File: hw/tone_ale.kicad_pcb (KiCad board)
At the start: 2 copper layers, 99.1 x 72.9 mm, 53 parts, among them J1 Conn_01x02, J2 USB_B_Micro, J3 Conn_01x02, J4 Conn_02x08_Odd_Even, J5 Conn_02x11_Odd_Even, U1 NCP1117-3.3_SOT223, U2 W25Q128JVS, U3 RP2040, U4 PCM5102, U5 PCM1808PWR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

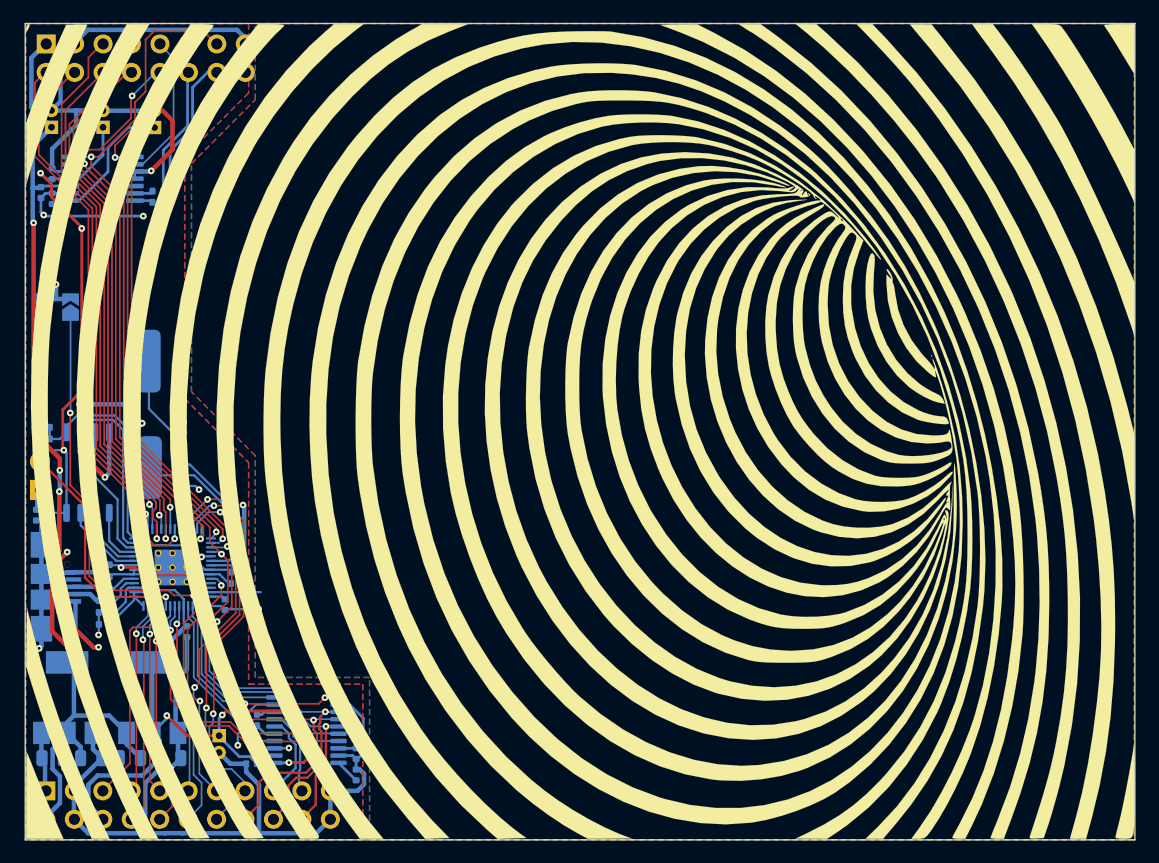
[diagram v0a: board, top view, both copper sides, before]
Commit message: Updated hardware. Made wah only engaged while foot is on pedal
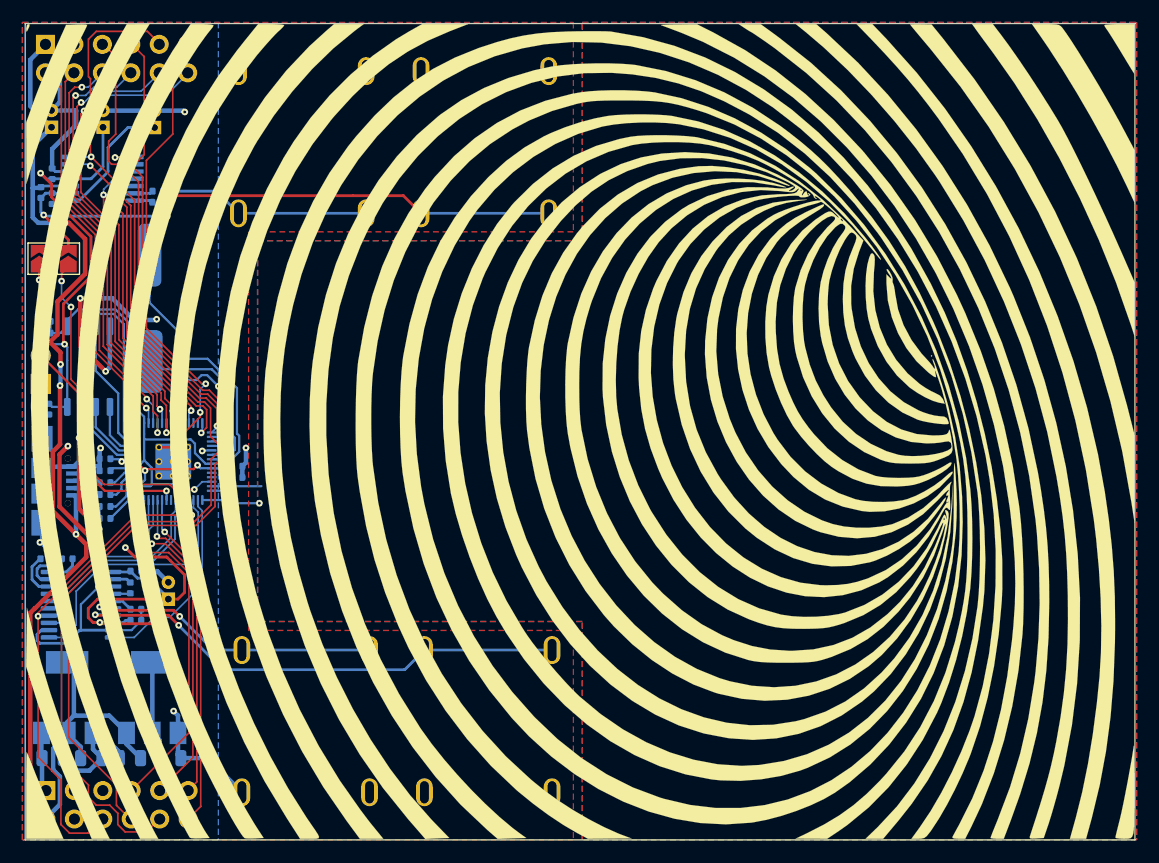
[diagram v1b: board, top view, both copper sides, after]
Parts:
- added J6: Conn_01x02, mylib:acjm_mhdr, B.Cu at (86.3, 121.9)
- added J7: Conn_01x02, mylib:acjm_mhdr, B.Cu at (86.0, 70.2)
- added J8: Conn_01x02, mylib:acjm_mhdr, B.Cu at (102.3, 70.2)
- added J9: Conn_01x02, mylib:acjm_mhdr, B.Cu at (102.6, 121.9)
- J1, J3: moved to F.Cu
- J4: value Conn_02x08_Odd_Even -> Conn_02x06_Odd_Even; footprint Connector_PinHeader_2.54mm:PinHeader_2x08_P2.54mm_Vertical -> Connector_PinHeader_2.54mm:PinHeader_2x06_P2.54mm_Vertical
- J5: value Conn_02x11_Odd_Even -> Conn_02x06_Odd_Even; footprint Connector_PinHeader_2.54mm:PinHeader_2x11_P2.54mm_Vertical -> Connector_PinHeader_2.54mm:PinHeader_2x06_P2.54mm_Vertical
- moved C21 32.7 mm to (63.1, 107.4), turned to 0 degrees
- moved C26 32.2 mm to (65.0, 107.4), turned to 180 degrees
- moved U4 23.0 mm to (66.2, 111.5), turned to 180 degrees
- moved C25 20.1 mm to (71.1, 108.5), turned to 0 degrees
- moved C20 18.2 mm to (70.6, 110.0), turned to -90 degrees
- moved C22 14.7 mm to (71.1, 111.9), turned to 0 degrees
- moved C27 13.3 mm to (71.1, 112.9), turned to 0 degrees
- moved C28 13.0 mm to (74.0, 111.0), turned to 90 degrees
- moved C12 9.47 mm to (75.4, 104.4)
- moved C1 9.46 mm to (75.5, 91.0)
- moved C10 9.46 mm to (68.4, 103.8)
- moved C11 9.46 mm to (71.2, 93.5)
- moved C2 9.46 mm to (75.5, 87.2)
- moved C4 9.46 mm to (63.4, 94.0)
- moved C6 9.46 mm to (68.4, 98.5)
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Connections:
- J4 pad 10: /gp5 -> /gp4
- J4 pad 11: /i2cv_clk -> /gp6
- J4 pad 12: VINL -> /gp5
- J4 pad 2: /gp6 -> /gp0
- J4 pad 4: /gp0 -> /gp1
- J4 pad 5: /gp1 -> /i2cv_in
- J4 pad 7: /gp3 -> /i2cv_clk
- J4 pad 8: /gp4 -> /gp3
- J4 pad 9: /i2cv_in -> /i2cv_ws
- J5 pad 10: /pot0 -> /i2cv_ws
- J5 pad 11: /swd -> /pot1
- J5 pad 12: /gp10 -> /pot0
- J5 pad 5: /gp24 -> +3V3
- J5 pad 6: +3V3 -> /i2cv_out
- J5 pad 8: /pot2 -> /i2cv_clk
- J5 pad 9: /pot1 -> /pot2
- U3 pad 11: /gp8 -> /adc_md1
- U3 pad 9: unconnected-(U3-Pad9) -> /adc_md0
- U5 pad 10: GND -> /adc_md0
- U5 pad 11: GND -> /adc_md1
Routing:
- net GND: track 219.9 -> 170.3 mm, vias 17 -> 18
- net VOUTR: track 7.84 -> 45.2 mm, vias 0 -> 2
- net /gp9: track 35.3 -> 0.00 mm, vias 2 -> 0
- net /gp8: track 34.6 -> 0.00 mm, vias 2 -> 0
- net /gp10: track 33.3 -> 0.00 mm, vias 2 -> 0
- net /adc_md0: track 0.00 -> 27.1 mm, vias 0 -> 2
- net /adc_md1: track 0.00 -> 26.6 mm, vias 0 -> 2
- net /swclk: track 22.1 -> 0.00 mm, vias 2 -> 0
- net /gp24: track 21.6 -> 0.00 mm, vias 1 -> 0
- net VINR: track 14.0 -> 35.3 mm, vias 0 -> 1
- net /swd: track 20.6 -> 0.00 mm, vias 2 -> 0
- net VOUTL: track 7.73 -> 26.9 mm, vias 0 -> 2
- net VBUS: track 95.2 -> 113.5 mm
- net /pot3: track 17.1 -> 30.9 mm
- net +3V3: track 147.2 -> 133.6 mm, vias 10 -> 7
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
